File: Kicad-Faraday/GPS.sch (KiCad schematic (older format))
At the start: 19 parts, among them U7 M10478-A2

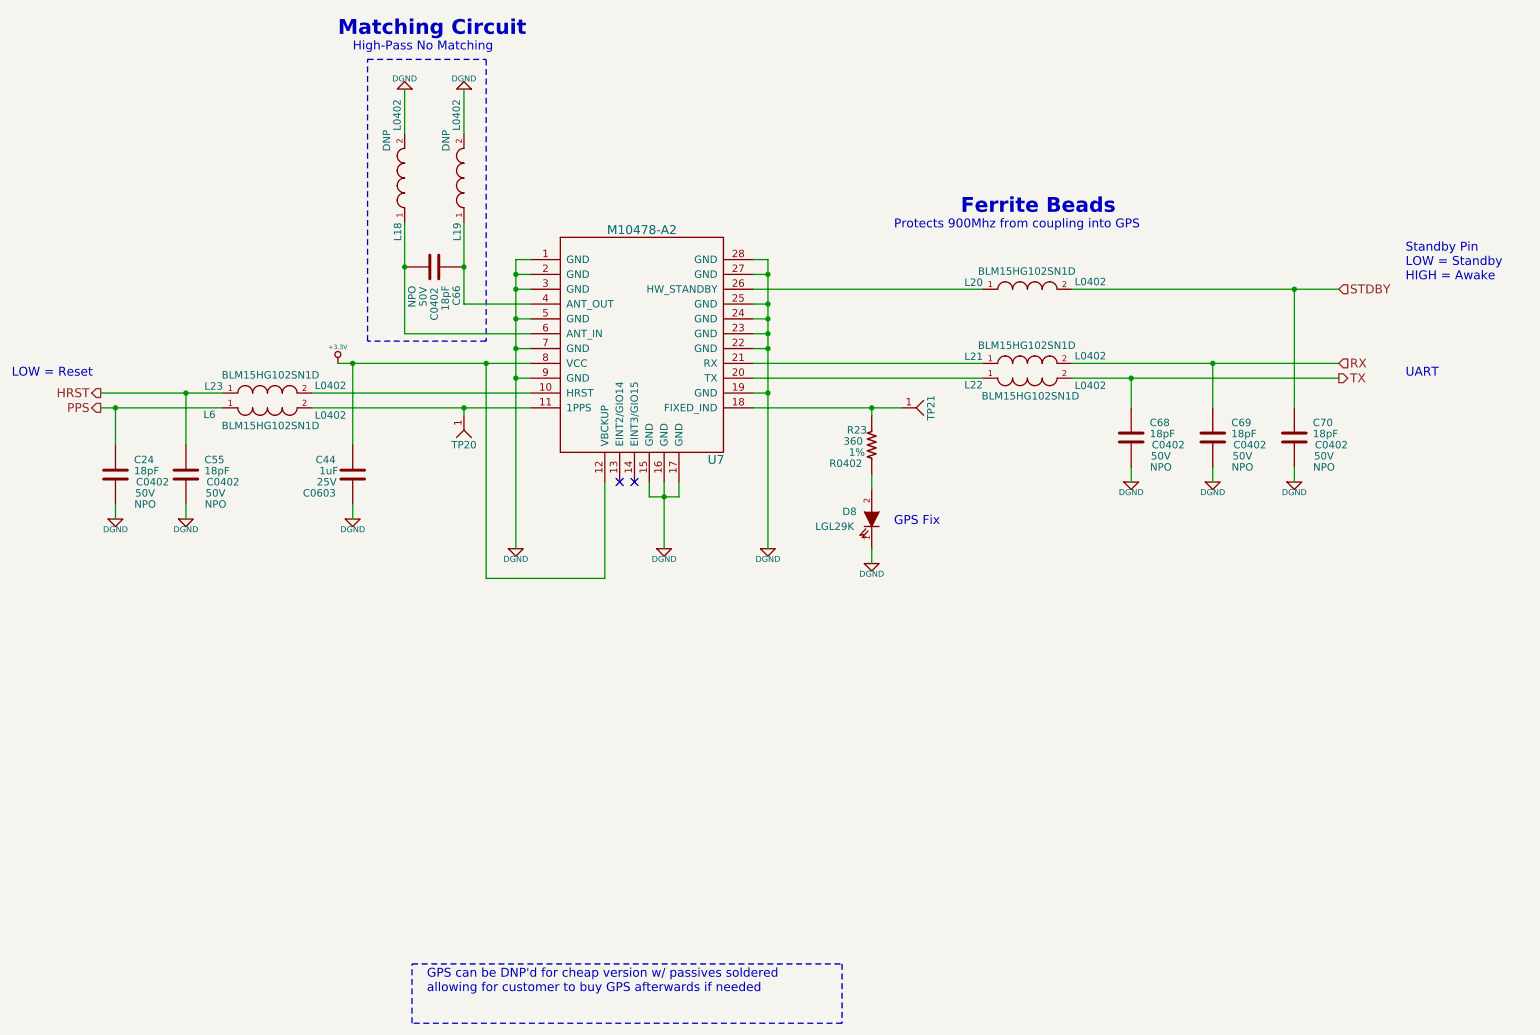
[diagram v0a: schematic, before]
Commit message: Updated per RevD Github Issue comments. Largely removed unnecessary items
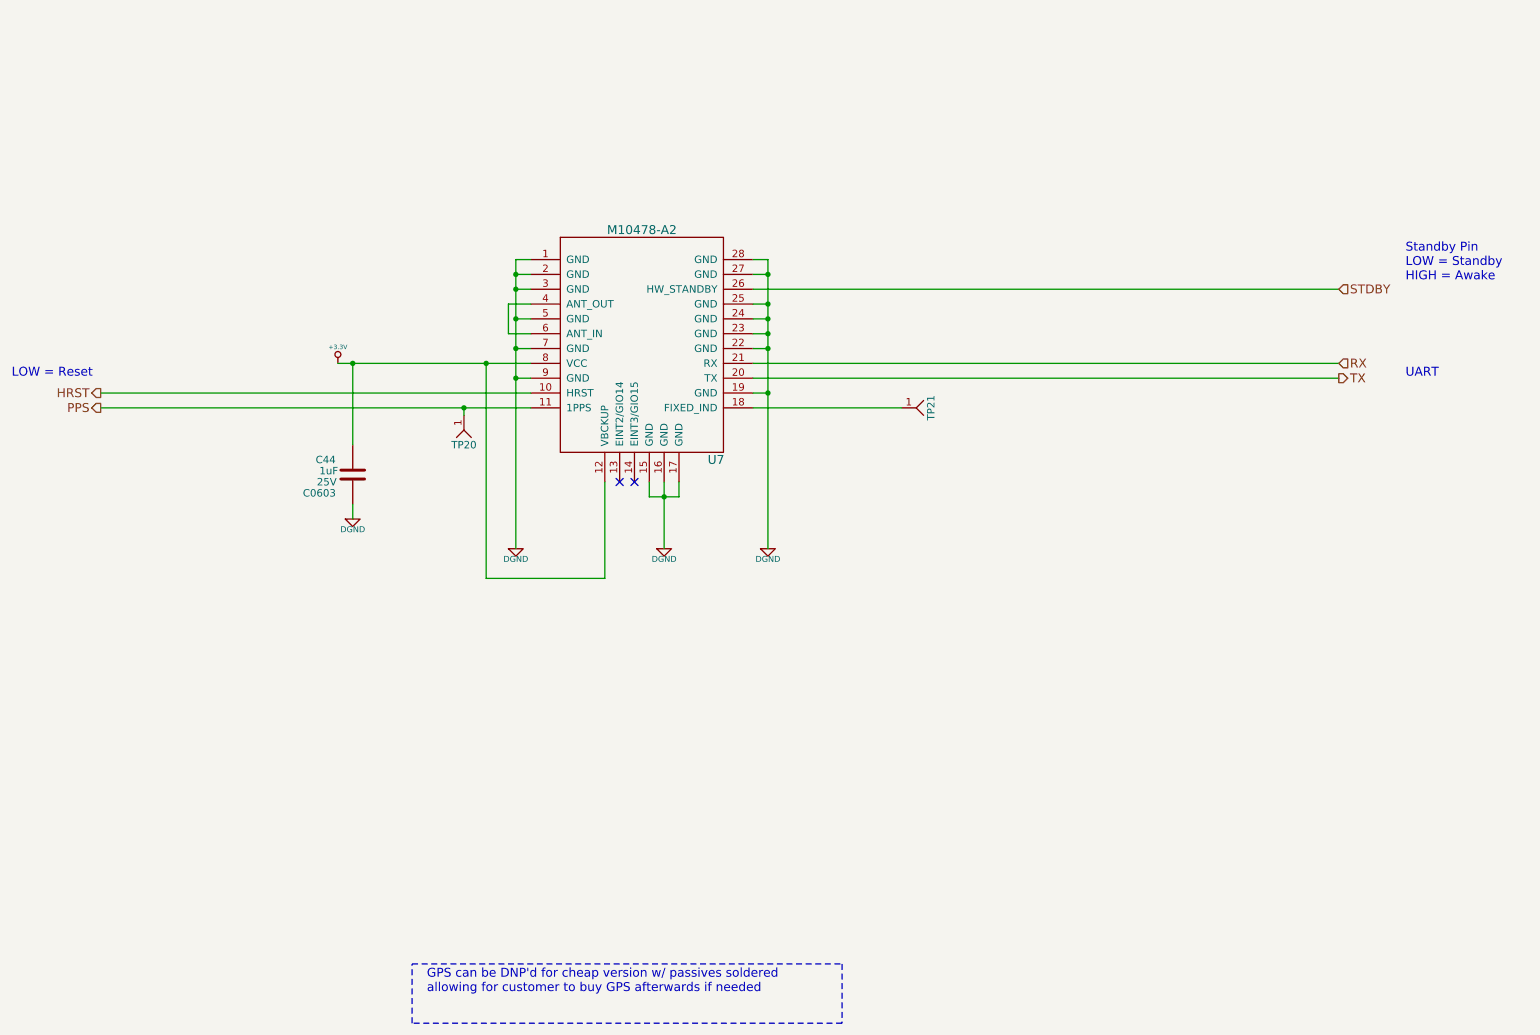
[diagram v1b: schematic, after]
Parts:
- removed C24, C55, C66, C68, C69, C70: 18pF, C0402, symbol C
- removed D8: LED-IPC, LGL29K, symbol LED-IPC
- removed L18, L19: DNP, L0402, symbol L-US
- removed L20, L21, L22, L23, L6: BLM15HG102SN1D, L0402, symbol L-US
- removed R23: 360, R0402, symbol R_US
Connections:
- net HRST: now also U7.10 (HRST)
- net PPS: now also TP20.1, U7.11 (1PPS)
- net RX: now also U7.21 (RX)
- net STDBY: now also U7.26 (HW_STANDBY)
- net TX: now also U7.20 (TX)
- net at U7.4 (ANT_OUT): now also U7.6 (ANT_IN)
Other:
- note removed: "Ferrite Beads"
- note removed: "GPS Fix"
- note removed: "High-Pass No Matching"
- note removed: "Matching Circuit"
- note removed: "Protects 900Mhz from coupling into GPS"
